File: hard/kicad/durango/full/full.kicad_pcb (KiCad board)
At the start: 2 copper layers, 97 parts, among them J1 NANOLINK, J105 SCART, J206 VIDEO, J3 IOX9, J4 BUZZER, J7 5V DC, J8 DEBUG, Q1 BC547, Q106 BC547, Q2 BC547, Q3 BC547, Q4 BC547, Q5 BC547, SW1 RESET, SW2 NMI, U1 65C02, U10 74HC139, U104 74HC257, U105 74HC257, U11 74HC688, U12 74HC74, U124 74HC574, U125 74HC257, U126 HC86, U127 74HC245, U13 74HC32, U14 74HC4024, U15 74HCT4040, U16 74HC02, U17 74HC21, U18 74HC85, U19 74HC4040, U2 27C256, U20 74HC85, U204 74HC257, U205 74HC257, U22 74HC175, U224 74HC166, U227 74HC20, U23 74HC86, U3 62256, U31 74HC245, U32 74HC365, U321 74HC257, U528 74HC174, U529 74HC139, U530 74HC367, U6 74HC257, U7 74HC257, U8 74HC132, U9 74HC00, X1 24.576 MHz

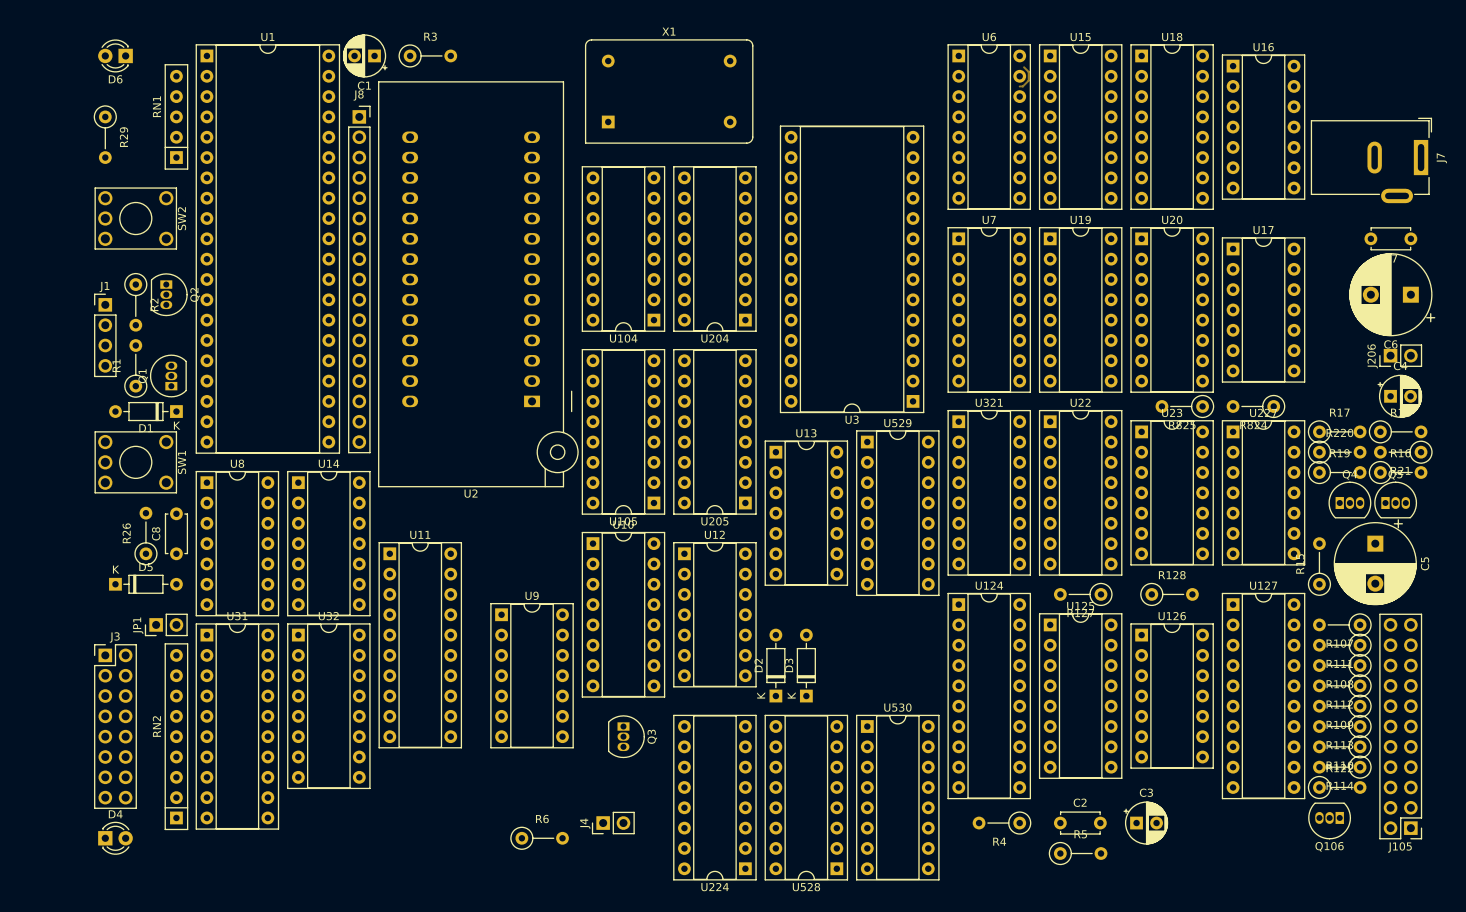
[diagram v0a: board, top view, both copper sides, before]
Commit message: smaller resistors in Durango-X
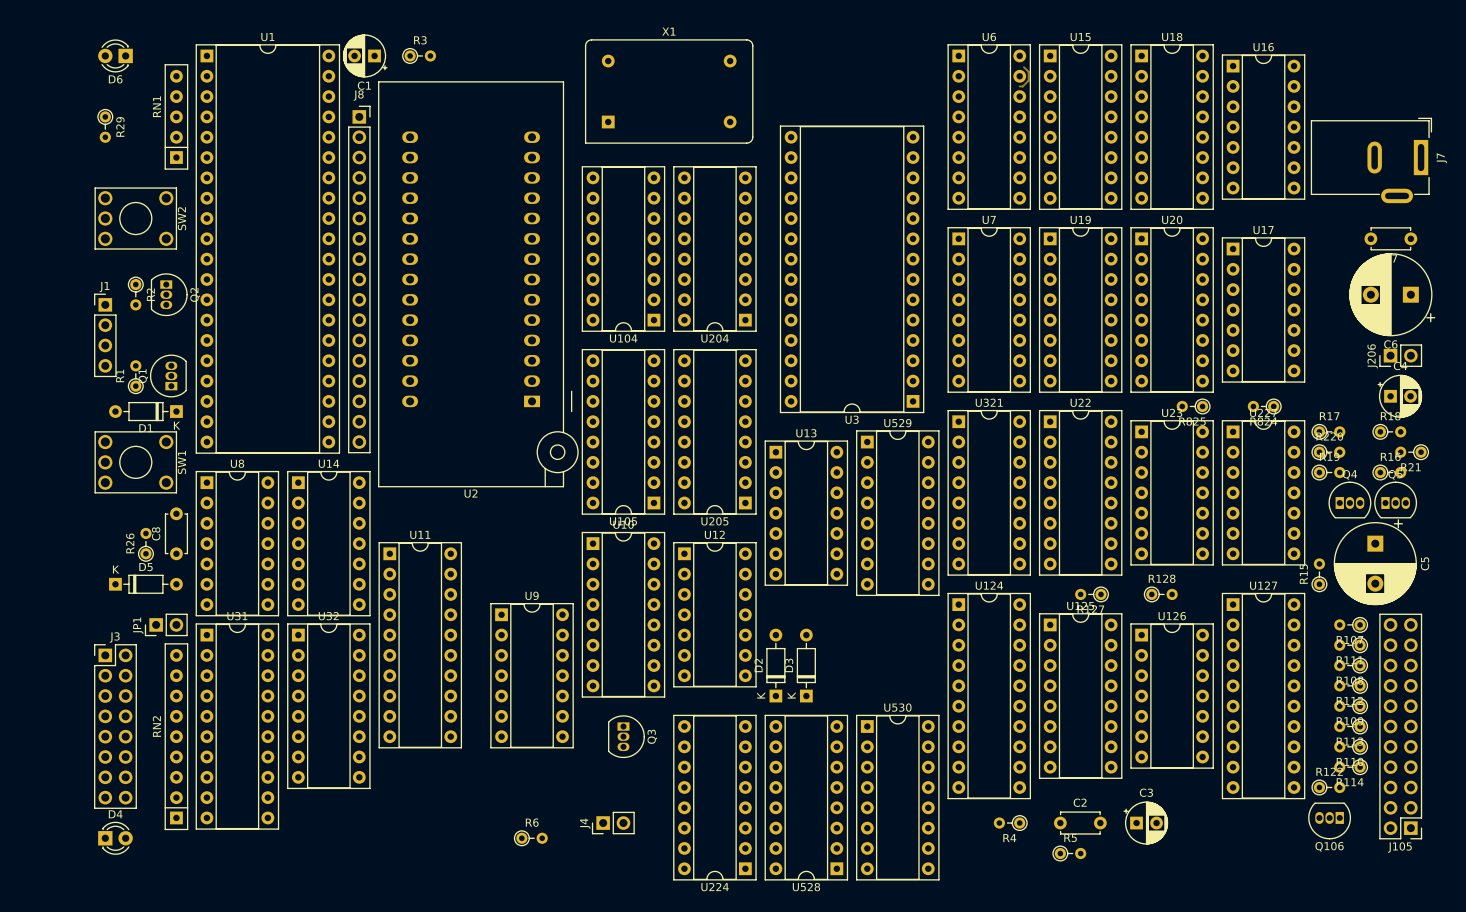
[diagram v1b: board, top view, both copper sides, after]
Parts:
- R1, R107, R108, R109, R110, R111, R112, R113, R114, R122, R127, R128, R15, R16, R17, R18, R19, R2, R21, R220, R26, R29, R3, R4, R5, R6, R824, R825: footprint Resistor_THT:R_Axial_DIN0207_L6.3mm_D2.5mm_P5.08mm_Vertical -> Resistor_THT:R_Axial_DIN0204_L3.6mm_D1.6mm_P2.54mm_Vertical

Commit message: some new footprints in Durango-X
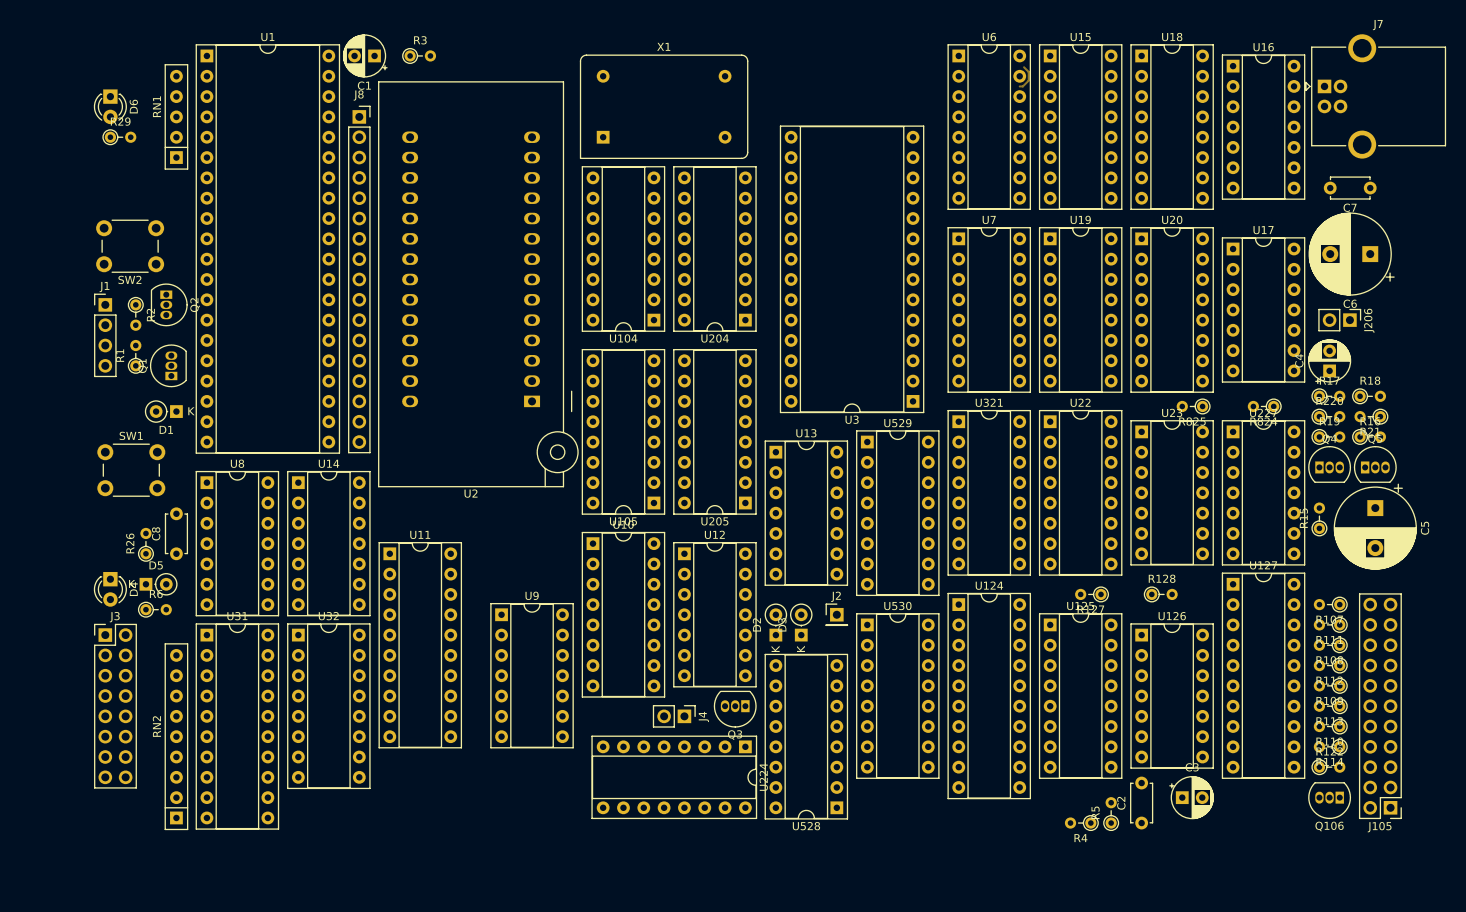
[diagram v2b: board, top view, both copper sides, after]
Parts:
- removed JP1: AUDIO FEEDBACK, Connector_PinHeader_2.54mm:PinHeader_1x02_P2.54mm_Vertical
- added J2: AUDIO IN, Connector_PinHeader_2.54mm:PinHeader_1x01_P2.54mm_Vertical, F.Cu at (153.7, 118.1)
- D1, D2, D3, D5: footprint Diode_THT:D_DO-35_SOD27_P7.62mm_Horizontal -> Diode_THT:D_DO-35_SOD27_P2.54mm_Vertical_KathodeUp
- J7: value 5V DC -> POWER; footprint Connector_BarrelJack:BarrelJack_Wuerth_6941xx301002 -> Connector_USB:USB_B_OST_USB-B1HSxx_Horizontal
- SW1, SW2: footprint Button_Switch_THT:KSA_Tactile_SPST -> Button_Switch_THT:SW_PUSH_6mm
- moved R6 55.0 mm to (67.3, 117.5)
- moved D4 32.4 mm to (62.9, 113.7), turned to 270 degrees
- moved J4 16.8 mm to (134.6, 130.8), turned to 270 degrees
- moved Q3 15.5 mm to (142.2, 129.5), turned to 180 degrees
- moved U224 15.2 mm to (142.2, 134.6), turned to 270 degrees
- moved J7 15.0 mm to (214.6, 52.1), turned to 0 degrees
- moved U530 12.7 mm to (157.5, 119.4)
- moved C2 10.2 mm to (191.8, 144.1), turned to 90 degrees
- moved R4 8.89 mm to (185.4, 144.1)
- moved SW2 8.35 mm to (68.6, 74.3), turned to 180 degrees
- moved C4 8.26 mm to (215.3, 87.6), turned to 90 degrees
- moved C7 8.13 mm to (220.3, 64.8)
- moved SW1 7.73 mm to (62.2, 97.8), turned to 0 degrees
- moved D3 7.65 mm to (149.2, 120.7)
- moved D2 7.62 mm to (146.1, 120.7)
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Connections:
- J7 pad 2: GND -> (no net)

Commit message: some routing
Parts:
- moved D6 3.17 mm to (64.8, 55.9)
- moved R29 3.17 mm to (64.8, 61.0)
- moved D4 2.01 mm to (64.8, 114.3)
- moved R6 1.42 mm to (68.6, 116.8)
- moved D5 1.27 mm to (68.6, 114.3)
- moved SW2 0.64 mm to (68.6, 73.7)
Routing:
- net D2: track 0.00 -> 76.5 mm, vias 0 -> 2
- net D1: track 0.00 -> 75.9 mm, vias 0 -> 2
- net D0: track 0.00 -> 75.1 mm
- net A1: track 0.00 -> 70.5 mm
- net D3: track 0.00 -> 61.9 mm, vias 0 -> 2
- net A2: track 0.00 -> 61.9 mm
- net D4: track 0.00 -> 58.7 mm, vias 0 -> 2
- net A3: track 0.00 -> 58.0 mm
- net A4: track 0.00 -> 54.2 mm
- net A7: track 0.00 -> 54.2 mm
- net A6: track 0.00 -> 54.2 mm
- net A5: track 0.00 -> 54.2 mm
- net A0: track 0.00 -> 50.4 mm
- net A10: track 0.00 -> 45.1 mm, vias 0 -> 2
- net A11: track 0.00 -> 29.7 mm, vias 0 -> 2
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
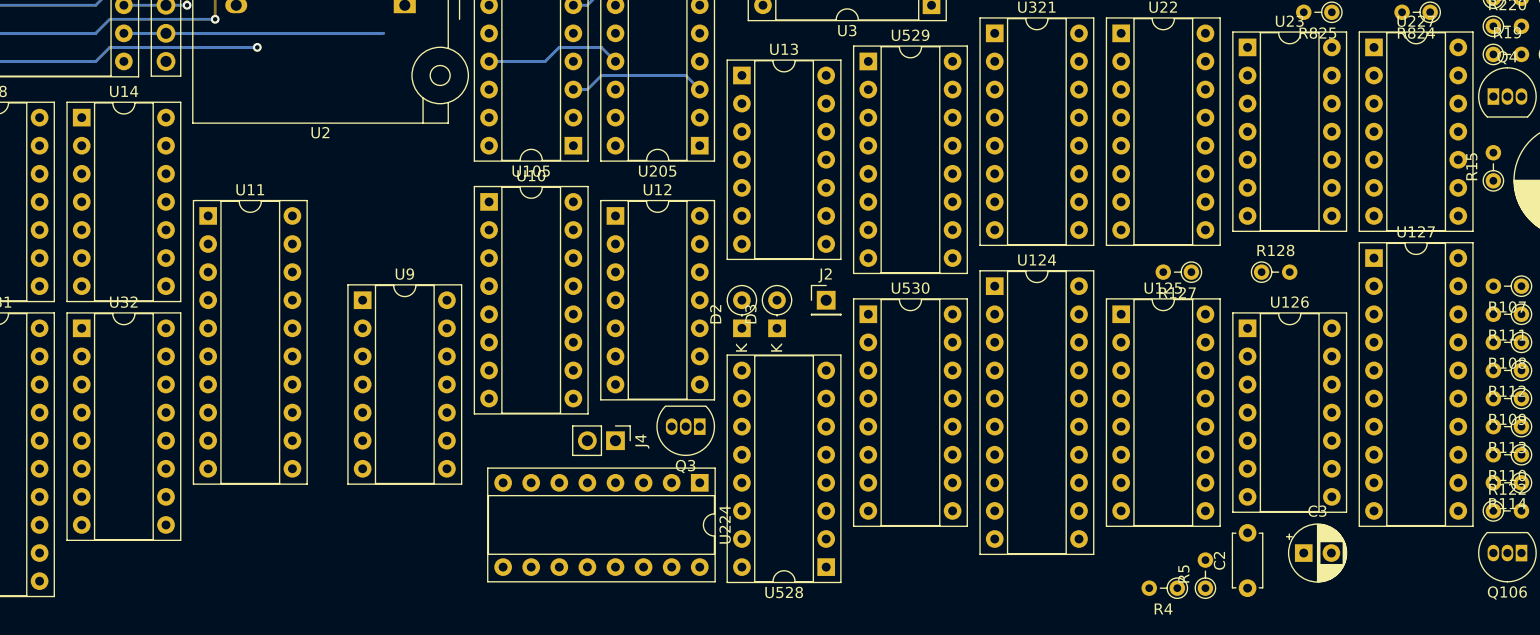
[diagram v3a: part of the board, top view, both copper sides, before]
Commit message: back to 4040 IRQ generator
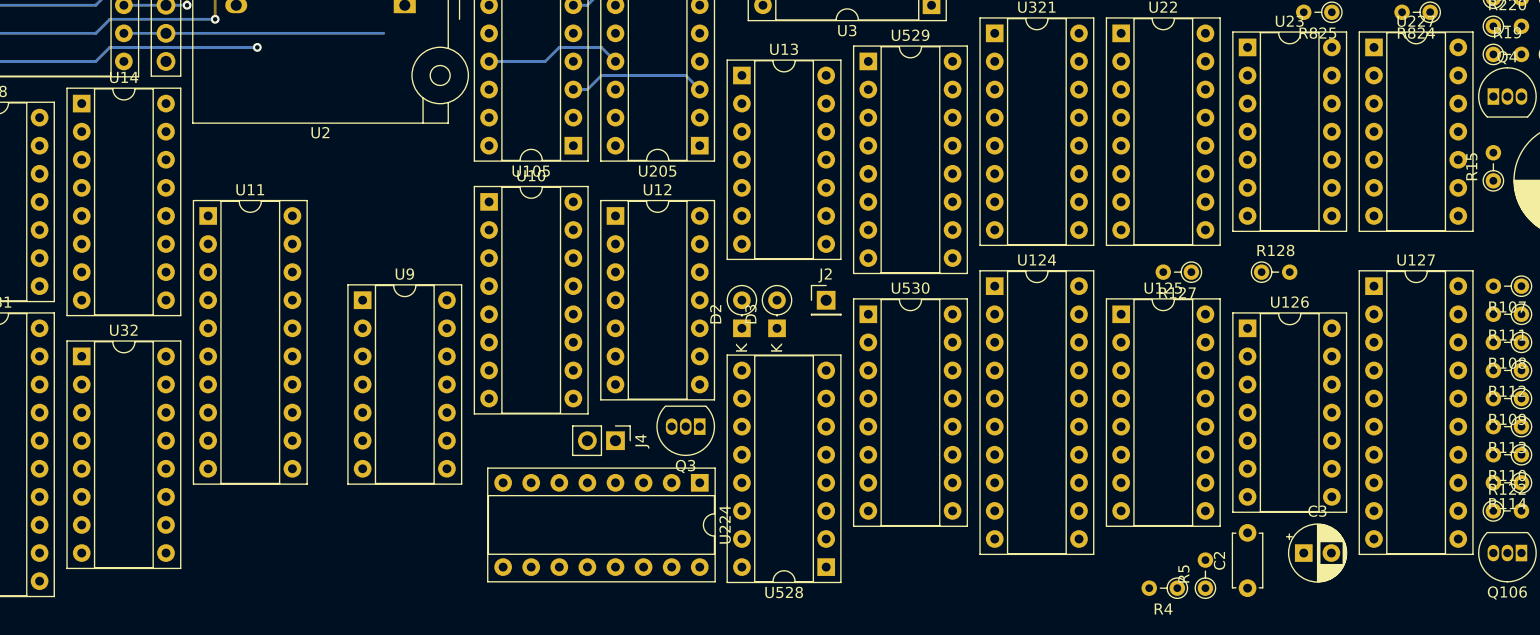
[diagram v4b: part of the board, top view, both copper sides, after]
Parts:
- R26: value 130K -> 220K
- U14: value 74HC4024 -> 74HC4040; footprint Package_DIP:DIP-14_W7.62mm_Socket -> Package_DIP:DIP-16_W7.62mm_Socket
- moved U127 2.54 mm to (203.2, 116.8)
- moved U32 2.54 mm to (86.4, 123.2)
- moved U14 1.27 mm to (86.4, 100.3)
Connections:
- U14 pad 1: VA5 -> Net-(U14-Pad1)
- U14 pad 10: (no net) -> VA0
- U14 pad 11: (no net) -> /HZ250
- U14 pad 14: +5V -> (no net)
- U14 pad 2: /HZ250 -> (no net)
- U14 pad 3: Net-(U14-Pad3) -> (no net)
- U14 pad 4: Net-(U14-Pad4) -> (no net)
- U14 pad 7: GND -> (no net)
- U14 pad 8: (no net) -> GND
- U8 pad 1: Net-(U14-Pad3) -> Net-(U14-Pad1)
- U8 pad 2: Net-(U14-Pad4) -> Net-(U14-Pad15)

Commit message: more delay resistors and BOM optimisation
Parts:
- added R229: 0, Resistor_THT:R_Axial_DIN0204_L3.6mm_D1.6mm_P2.54mm_Vertical, F.Cu at (191.8, 92.1)
- C1: value 1uF* -> 1uF
- C6: value 1000uF -> 470uF
- C8: value 33pF -> 68pF
- J1: footprint Connector_PinHeader_2.54mm:PinHeader_1x04_P2.54mm_Vertical -> Connector_Audio:Jack_3.5mm_CUI_SJ1-3533NG_Horizontal_CircularHoles
- R3: value 1K* -> 22K
- R824, R825: value 68K -> 220K
- moved J1 28.8 mm to (55.2, 51.4)
- moved R824 2.54 mm to (205.7, 92.1)
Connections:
- net Net-(U227-Pad9) renamed /VDU-X/HVID
- U227 pad 10: /VDU-X/HRDE -> /VDU-X/DHRDE
- U9 pad 1: SCLK -> VCLK
- U9 pad 5: SCLK -> VCLK
